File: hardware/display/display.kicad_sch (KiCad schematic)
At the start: 420 parts, among them J1 Power Connector, J2 Data Connector

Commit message: Arranged/Routed 100uF Bulk Caps
Manually routed each of the 10 caps by deleting 2 common NoePixel vias to make room for the pad, orienting the cap so VDD/GND is next to the deleted vias, and then routed VDD/GND into the one big via from the NeoPixels.
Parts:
- C81, C82, C83, C84, C85, C86, C87, C88, C89, C90: footprint esp32_handheld:CAP_TAJ-D- 2917-S_AVX -> esp32_handheld:CAP_TAJ-D- 2917-S_AVX_NO_RESTRICTION
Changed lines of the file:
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@@
 			)
 		)
-		(property "Footprint" "esp32_handheld:CAP_TAJ-D- 2917-S_AVX"
+		(property "Footprint" "esp32_handheld:CAP_TAJ-D- 2917-S_AVX_NO_RESTRICTION"
 			(at 402.59 229.87 0)
 			(effects
@@
 			)
 		)
-		(property "Footprint" "esp32_handheld:CAP_TAJ-D- 2917-S_AVX"
+		(property "Footprint" "esp32_handheld:CAP_TAJ-D- 2917-S_AVX_NO_RESTRICTION"
 			(at 443.23 229.87 0)
 			(effects
@@
 			)
 		)
-		(property "Footprint" "esp32_handheld:CAP_TAJ-D- 2917-S_AVX"
+		(property "Footprint" "esp32_handheld:CAP_TAJ-D- 2917-S_AVX_NO_RESTRICTION"
 			(at 412.75 229.87 0)
 			(effects
@@
 			)
 		)
-		(property "Footprint" "esp32_handheld:CAP_TAJ-D- 2917-S_AVX"
+		(property "Footprint" "esp32_handheld:CAP_TAJ-D- 2917-S_AVX_NO_RESTRICTION"
 			(at 392.43 229.87 0)
 			(effects
@@
 			)
 		)
-		(property "Footprint" "esp32_handheld:CAP_TAJ-D- 2917-S_AVX"
+		(property "Footprint" "esp32_handheld:CAP_TAJ-D- 2917-S_AVX_NO_RESTRICTION"
 			(at 433.07 229.87 0)
 			(effects
@@
 			)
 		)
-		(property "Footprint" "esp32_handheld:CAP_TAJ-D- 2917-S_AVX"
+		(property "Footprint" "esp32_handheld:CAP_TAJ-D- 2917-S_AVX_NO_RESTRICTION"
 			(at 351.79 229.87 0)
 			(effects
@@
 			)
 		)
-		(property "Footprint" "esp32_handheld:CAP_TAJ-D- 2917-S_AVX"
+		(property "Footprint" "esp32_handheld:CAP_TAJ-D- 2917-S_AVX_NO_RESTRICTION"
 			(at 422.91 229.87 0)
 			(effects
@@
 			)
 		)
-		(property "Footprint" "esp32_handheld:CAP_TAJ-D- 2917-S_AVX"
+		(property "Footprint" "esp32_handheld:CAP_TAJ-D- 2917-S_AVX_NO_RESTRICTION"
 			(at 372.11 229.87 0)
 			(effects
@@
 			)
 		)
-		(property "Footprint" "esp32_handheld:CAP_TAJ-D- 2917-S_AVX"
+		(property "Footprint" "esp32_handheld:CAP_TAJ-D- 2917-S_AVX_NO_RESTRICTION"
 			(at 361.95 229.87 0)
 			(effects
@@
 			)
 		)
-		(property "Footprint" "esp32_handheld:CAP_TAJ-D- 2917-S_AVX"
+		(property "Footprint" "esp32_handheld:CAP_TAJ-D- 2917-S_AVX_NO_RESTRICTION"
 			(at 382.27 229.87 0)
 			(effects

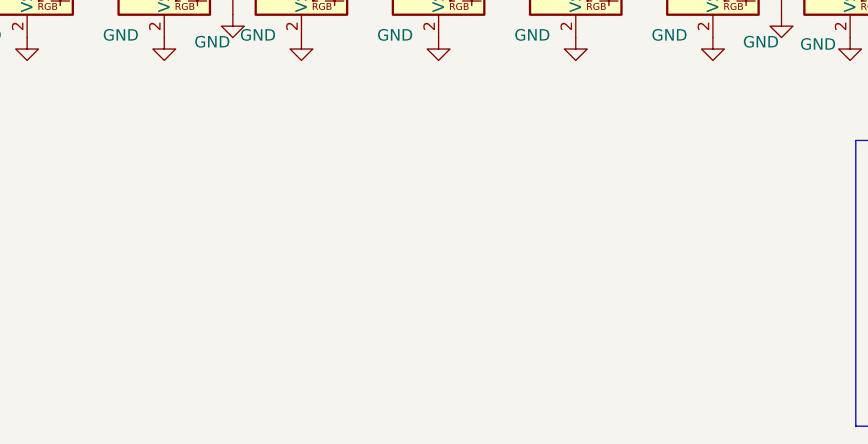
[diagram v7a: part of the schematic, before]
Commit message: Added Real Mounting Holes and Fiducial
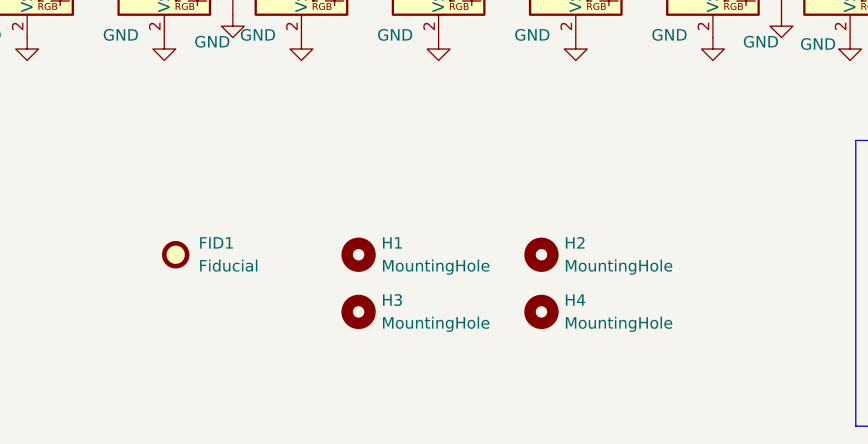
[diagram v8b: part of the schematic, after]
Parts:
- added FID1: Fiducial, Fiducial:Fiducial_1mm_Mask2mm, symbol Mechanical:Fiducial
- added H1, H2, H3, H4: MountingHole, MountingHole:MountingHole_3.2mm_M3_DIN965_Pad, symbol Mechanical:MountingHole
